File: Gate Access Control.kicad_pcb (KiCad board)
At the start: 2 copper layers, 85.1 x 38 mm, 20 parts, among them J1 Screw_Terminal_01x02, J2 RF Receiver 433MHz, J3 Conn_01x08, J4 IR_SENSORT, J5 Screw_Terminal_01x04, J6 Screw_Terminal_01x02, J7 Screw_Terminal_01x02, J8 Conn_01x06, U1 ATmega328-MM, Y1 Crystal

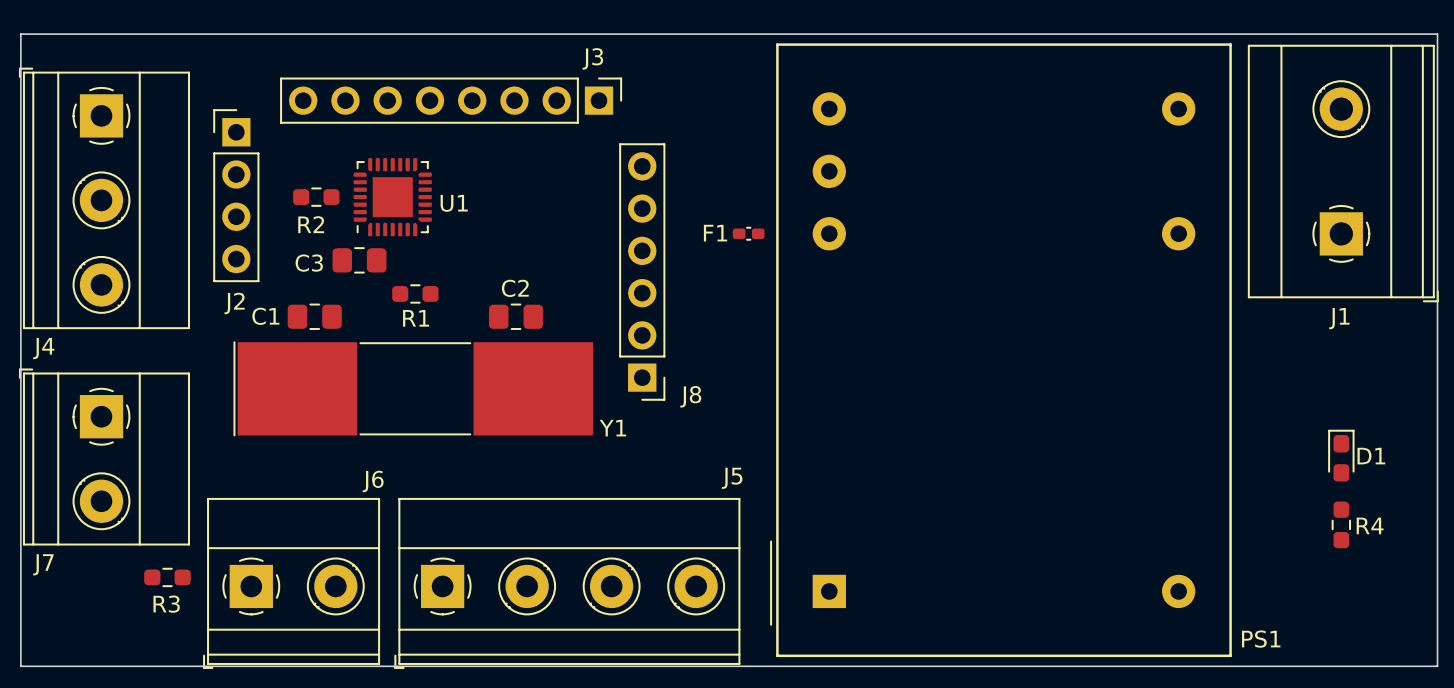
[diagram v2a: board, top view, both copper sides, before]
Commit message: Routed the Signal Traces
Design #1
Also changed on pre-defined size for Power to 0.25mm.
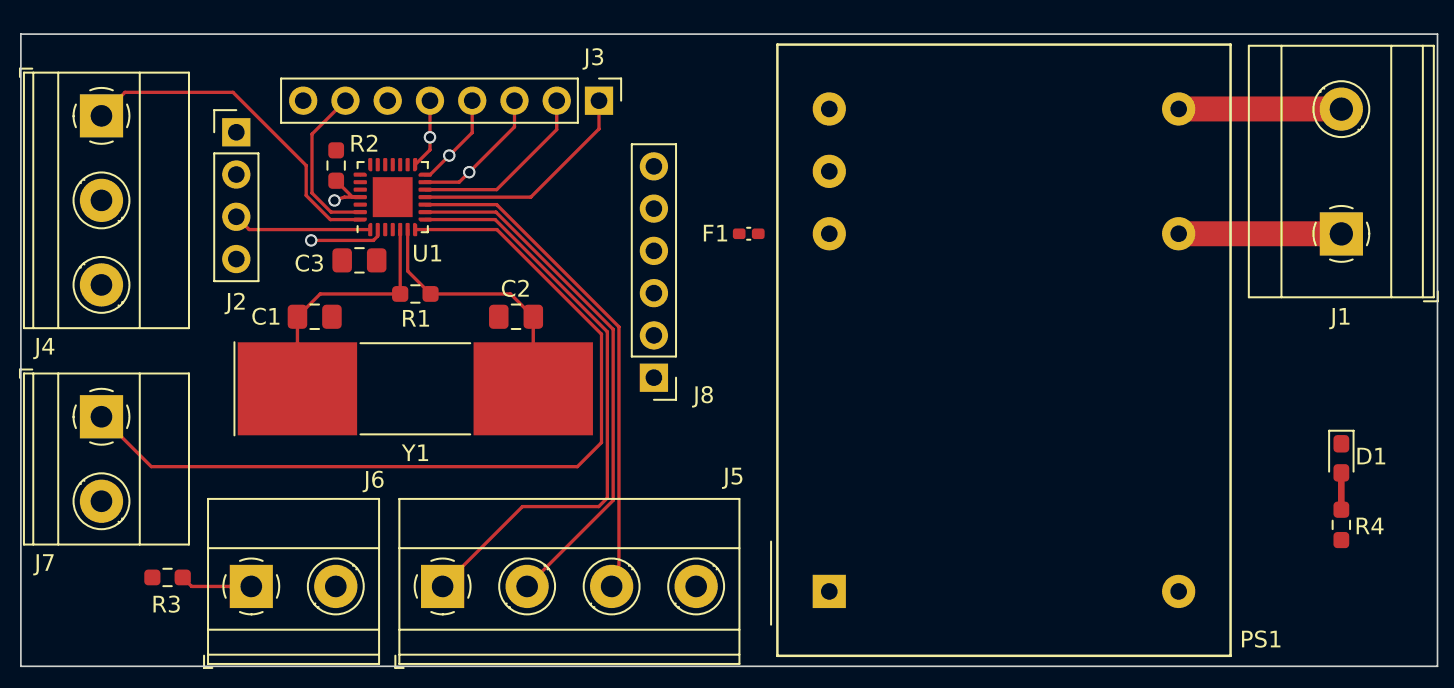
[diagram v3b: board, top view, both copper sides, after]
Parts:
- moved R2 2.24 mm to (71.5, 62.9), turned to 90 degrees
- moved J8 0.70 mm to (90.6, 75.7)
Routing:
- net /Flashing Lights: track 0.00 -> 52.2 mm
- net /Inverter PWM: track 0.00 -> 35.8 mm
- net /Enable: track 0.00 -> 31.8 mm
- net /DXN: track 0.00 -> 30.5 mm
- net /IR Sensor - DI: track 0.00 -> 20.4 mm
- net /XTAL2: track 0.00 -> 15.5 mm
- net /XTAL1: track 0.00 -> 14.9 mm
- net /RST: track 0.00 -> 13.8 mm
- net /SDA/SS: track 0.00 -> 11.1 mm
- net Net-(J1-Pin_1): track 0.00 -> 9.78 mm
- net Net-(J1-Pin_2): track 0.00 -> 9.78 mm
- net /IRQ: track 0.00 -> 9.76 mm
- net /Switch IN: track 0.00 -> 8.85 mm, vias 0 -> 1
- net /RF receiver - PWM: track 0.00 -> 8.37 mm
- net /MOSI: track 0.00 -> 8.33 mm, vias 0 -> 1
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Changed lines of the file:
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@@
   )
   (paper "A4")
+  (title_block
+    (title "George-PCB")
+  )
   (layers
     (0 "F.Cu" signal)
@@
   (net 31 "unconnected-(U1-PD0-Pad26)")
   (footprint "Connector_PinHeader_2.54mm:PinHeader_1x06_P2.54mm_Vertical" (layer "F.Cu")
-    (at 89.9 75.65 180)
+    (at 90.6 75.65 180)
     (descr "Through hole straight pin header, 1x06, 2.54mm pitch, single row")
     (tags "Through hole pin header THT 1x06 2.54mm single row")
@@
     (property "ki_keywords" "AVR 8bit Microcontroller MegaAVR")
     (attr smd)
-    (fp_text reference "U1" (at -0.4 3.7 180) (layer "F.SilkS")
+    (fp_text reference "U1" (at -3.4 2.1 180) (layer "F.SilkS")
         (effects (font (size 1 1) (thickness 0.15)))
     )
@@
     (property "ki_keywords" "quartz ceramic resonator oscillator")
     (attr smd)
-    (fp_text reference "Y1" (at 11.93875 2.4) (layer "F.SilkS")
+    (fp_text reference "Y1" (at 0.03875 3.88) (layer "F.SilkS")
         (effects (font (size 1 1) (thickness 0.15)))
     )
@@
   )
   (footprint "Resistor_SMD:R_0603_1608Metric_Pad0.98x0.95mm_HandSolder" (layer "F.Cu")
-    (at 70.31125 64.8 180)
+    (at 71.5 62.9 90)
     (descr "Resistor SMD 0603 (1608 Metric), square (rectangular) end terminal, IPC_7351 nominal with elongated pad for handsoldering. (Body size source: IPC-SM-782 page 72, https://www.pcb-3d.com/wordpress/wp-content/uploads/ipc-sm-782a_amendment_1_and_2.pdf), generated with kicad-footprint-generator")
     (tags "resistor handsolder")
@@
     (property "ki_keywords" "R res resistor")
     (attr smd)
-    (fp_text reference "R2" (at 0.31125 -1.7 180) (layer "F.SilkS")
-        (effects (font (size 1 1) (thickness 0.15)))
-    )
-    (fp_text value "1M" (at 0 1.43) (layer "F.Fab")
-        (effects (font (size 1 1) (thickness 0.15)))
-    )
-    (fp_text user "${REFERENCE}" (at 0 0) (layer "F.Fab")
+    (fp_text reference "R2" (at 1.3 1.7 180) (layer "F.SilkS")
+        (effects (font (size 1 1) (thickness 0.15)))
+    )
+    (fp_text value "1M" (at 0 1.43 90) (layer "F.Fab")
+        (effects (font (size 1 1) (thickness 0.15)))
+    )
+    (fp_text user "${REFERENCE}" (at 0 0 90) (layer "F.Fab")
         (effects (font (size 0.4 0.4) (thickness 0.06)))
     )
@@
     (fp_line (start 0.8 0.4125) (end -0.8 0.4125)
       (stroke (width 0.1) (type solid)) (layer "F.Fab"))
-    (pad "1" smd roundrect (at -0.9125 0 180) (size 0.975 0.95) (layers "F.Cu" "F.Paste" "F.Mask") (roundrect_rratio 0.25)
+    (pad "1" smd roundrect (at -0.9125 0 90) (size 0.975 0.95) (layers "F.Cu" "F.Paste" "F.Mask") (roundrect_rratio 0.25)
       (net 24 "/RESET") (pintype "passive"))
-    (pad "2" smd roundrect (at 0.9125 0 180) (size 0.975 0.95) (layers "F.Cu" "F.Paste" "F.Mask") (roundrect_rratio 0.25)
+    (pad "2" smd roundrect (at 0.9125 0 90) (size 0.975 0.95) (layers "F.Cu" "F.Paste" "F.Mask") (roundrect_rratio 0.25)
       (net 4 "+5V") (pintype "passive"))
     (model "${KICAD6_3DMODEL_DIR}/Resistor_SMD.3dshapes/R_0603_1608Metric.wrl"
@@
   (gr_rect (start 52.55 55) (end 137.7 93)
     (stroke (width 0.1) (type default)) (fill none) (layer "Edge.Cuts"))
+  (segment (start 69.17375 76.32) (end 69.17375 71.99) (width 0.2) (layer "F.Cu") (net 2))
+  (segment (start 70.54375 70.62) (end 75.35 70.62) (width 0.2) (layer "F.Cu") (net 2))
+  (segment (start 69.17375 71.99) (end 70.54375 70.62) (width 0.2) (layer "F.Cu") (net 2))
+  (segment (start 75.35 70.62) (end 75.35 66.75) (width 0.2) (layer "F.Cu") (net 2))
+  (segment (start 83.34875 76.32) (end 83.34875 71.9925) (width 0.2) (layer "F.Cu") (net 3))
+  (segment (start 77.175 70.62) (end 75.8 69.245) (width 0.2) (layer "F.Cu") (net 3))
+  (segment (start 75.8 69.245) (end 75.8 66.75) (width 0.2) (layer "F.Cu") (net 3))
+  (segment (start 81.98125 70.62) (end 83.35125 71.99) (width 0.2) (layer "F.Cu") (net 3))
+  (segment (start 83.34875 71.9925) (end 83.35125 71.99) (width 0.2) (layer "F.Cu") (net 3))
+  (segment (start 77.175 70.62) (end 81.98125 70.62) (width 0.2) (layer "F.Cu") (net 3))
+  (segment (start 131.92 81.375) (end 131.92 83.5875) (width 0.4) (layer "F.Cu") (net 5))
+  (segment (start 122.1425 67) (end 131.91 67) (width 1.5) (layer "F.Cu") (net 7))
+  (segment (start 131.91 67) (end 131.92 67.01) (width 1.5) (layer "F.Cu") (net 7))
+  (segment (start 122.1425 59.5) (end 131.91 59.5) (width 1.5) (layer "F.Cu") (net 8))
+  (segment (start 131.91 59.5) (end 131.92 59.51) (width 1.5) (layer "F.Cu") (net 8))
+  (segment (start 66.27 66.75) (end 73.55 66.75) (width 0.2) (layer "F.Cu") (net 10))
+  (segment (start 65.5 65.98) (end 66.27 66.75) (width 0.2) (layer "F.Cu") (net 10))
+  (segment (start 84.76 60.74) (end 81.15 64.35) (width 0.2) (layer "F.Cu") (net 11))
+  (segment (start 84.76 59) (end 84.76 60.74) (width 0.2) (layer "F.Cu") (net 11))
+  (segment (start 81.15 64.35) (end 76.85 64.35) (width 0.2) (layer "F.Cu") (net 11))
+  (segment (start 77.14 61.96) (end 76.25 62.85) (width 0.2) (layer "F.Cu") (net 12))
+  (segment (start 77.14 61.2) (end 77.14 61.96) (width 0.2) (layer "F.Cu") (net 12))
+  (segment (start 77.14 61.2) (end 77.14 59) (width 0.2) (layer "F.Cu") (net 12))
+  (via (at 77.14 61.2) (size 0.75) (drill 0.5) (layers "F.Cu" "B.Cu") (net 12))
+  (segment (start 78.9 63.9) (end 76.85 63.9) (width 0.2) (layer "F.Cu") (net 13))
+  (segment (start 79.5 63.3) (end 78.9 63.9) (width 0.2) (layer "F.Cu") (net 13))
+  (segment (start 82.22 60.58) (end 82.22 59) (width 0.2) (layer "F.Cu") (net 13))
+  (segment (start 79.5 63.3) (end 82.22 60.58) (width 0.2) (layer "F.Cu") (net 13))
+  (via (at 79.5 63.3) (size 0.75) (drill 0.5) (layers "F.Cu" "B.Cu") (net 13))
+  (segment (start 79.68 60.92) (end 79.68 59) (width 0.2) (layer "F.Cu") (net 14))
+  (segment (start 77.15 63.45) (end 76.85 63.45) (width 0.2) (layer "F.Cu") (net 14))
+  (segment (start 78.3 62.3) (end 79.68 60.92) (width 0.2) (layer "F.Cu") (net 14))
+  (segment (start 78.3 62.3) (end 77.15 63.45) (width 0.2) (layer "F.Cu") (net 14))
+  (via (at 78.3 62.3) (size 0.75) (drill 0.5) (layers "F.Cu" "B.Cu") (net 14))
+  (segment (start 72.95 65.7) (end 71.194974 65.7) (width 0.2) (layer "F.Cu") (net 15))
+  (segment (start 70.05 61.01) (end 72.06 59) (width 0.2) (layer "F.Cu") (net 15))
+  (segment (start 70.05 64.555026) (end 70.05 61.01) (width 0.2) (layer "F.Cu") (net 15))
+  (segment (start 71.194974 65.7) (end 70.05 64.555026) (width 0.2) (layer "F.Cu") (net 15))
+  (segment (start 76.85 64.8) (end 83.2 64.8) (width 0.2) (layer "F.Cu") (net 16))
+  (segment (start 87.3 60.7) (end 87.3 59) (width 0.2) (layer "F.Cu") (net 16))
+  (segment (start 83.2 64.8) (end 87.3 60.7) (width 0.2) (layer "F.Cu") (net 16))
+  (segment (start 71.15 66.15) (end 69.7 64.7) (width 0.2) (layer "F.Cu") (net 18))
+  (segment (start 58.81 58.5) (end 57.395 59.915) (width 0.2) (layer "F.Cu") (net 18))
+  (segment (start 69.7 64.7) (end 69.7 62.9) (width 0.2) (layer "F.Cu") (net 18))
+  (segment (start 69.7 62.9) (end 65.3 58.5) (width 0.2) (layer "F.Cu") (net 18))
+  (segment (start 65.3 58.5) (end 58.81 58.5) (width 0.2) (layer "F.Cu") (net 18))
+  (segment (start 72.95 66.15) (end 71.15 66.15) (width 0.2) (layer "F.Cu") (net 18))
+  (segment (start 88.15 72.744974) (end 88.15 83.03) (width 0.2) (layer "F.Cu") (net 19))
+  (segment (start 81.105026 65.7) (end 88.15 72.744974) (width 0.2) (layer "F.Cu") (net 19))
+  (segment (start 76.85 65.7) (end 81.105026 65.7) (width 0.2) (layer "F.Cu") (net 19))
+  (segment (start 88.15 83.03) (end 82.98 88.2) (width 0.2) (layer "F.Cu") (net 19))
+  (segment (start 82.7 83.4) (end 77.9 88.2) (width 0.2) (layer "F.Cu") (net 20))
+  (segment (start 87.8 82.885026) (end 87.285026 83.4) (width 0.2) (layer "F.Cu") (net 20))
+  (segment (start 81.060052 66.15) (end 87.8 72.889948) (width 0.2) (layer "F.Cu") (net 20))
+  (segment (start 87.285026 83.4) (end 82.7 83.4) (width 0.2) (layer "F.Cu") (net 20))
+  (segment (start 87.8 72.889948) (end 87.8 82.885026) (width 0.2) (layer "F.Cu") (net 20))
+  (segment (start 76.85 66.15) (end 81.060052 66.15) (width 0.2) (layer "F.Cu") (net 20))
+  (segment (start 81.15 65.25) (end 88.5 72.6) (width 0.2) (layer "F.Cu") (net 21))
+  (segment (start 88.5 87.76) (end 88.06 88.2) (width 0.2) (layer "F.Cu") (net 21))
+  (segment (start 88.5 72.6) (end 88.5 87.76) (width 0.2) (layer "F.Cu") (net 21))
+  (segment (start 76.85 65.25) (end 81.15 65.25) (width 0.2) (layer "F.Cu") (net 21))
+  (segment (start 73.741942 67.4) (end 70 67.4) (width 0.2) (layer "F.Cu") (net 22))
+  (segment (start 74 66.75) (end 74 67.141942) (width 0.2) (layer "F.Cu") (net 22))
+  (segment (start 74 67.141942) (end 73.741942 67.4) (width 0.2) (layer "F.Cu") (net 22))
+  (segment (start 62.2775 87.66) (end 62.8175 88.2) (width 0.2) (layer "F.Cu") (net 22))
+  (segment (start 62.8175 88.2) (end 66.4 88.2) (width 0.2) (layer "F.Cu") (net 22))
+  (via (at 70 67.4) (size 0.75) (drill 0.5) (layers "F.Cu" "B.Cu") (net 22))
+  (segment (start 87.45 79.55) (end 86 81) (width 0.2) (layer "F.Cu") (net 23))
+  (segment (start 76.25 66.75) (end 81.165078 66.75) (width 0.2) (layer "F.Cu") (net 23))
+  (segment (start 60.395 81) (end 57.395 78) (width 0.2) (layer "F.Cu") (net 23))
+  (segment (start 86 81) (end 60.395 81) (width 0.2) (layer "F.Cu") (net 23))
+  (segment (start 81.165078 66.75) (end 87.45 73.034922) (width 0.2) (layer "F.Cu") (net 23))
+  (segment (start 87.45 73.034922) (end 87.45 79.55) (width 0.2) (layer "F.Cu") (net 23))
+  (segment (start 72.4875 64.8) (end 71.5 63.8125) (width 0.2) (layer "F.Cu") (net 24))
+  (segment (start 72.95 64.8) (end 72 64.8) (width 0.2) (layer "F.Cu") (net 24))
+  (segment (start 71.4 65) (end 71.6 65.2) (width 0.2) (layer "F.Cu") (net 24))
+  (segment (start 72 64.8) (end 71.4 65) (width 0.2) (layer "F.Cu") (net 24))
+  (segment (start 72.95 64.8) (end 72.4875 64.8) (width 0.2) (layer "F.Cu") (net 24))
+  (via (at 71.4 65) (size 0.75) (drill 0.5) (layers "F.Cu" "B.Cu") (net 24))
 )

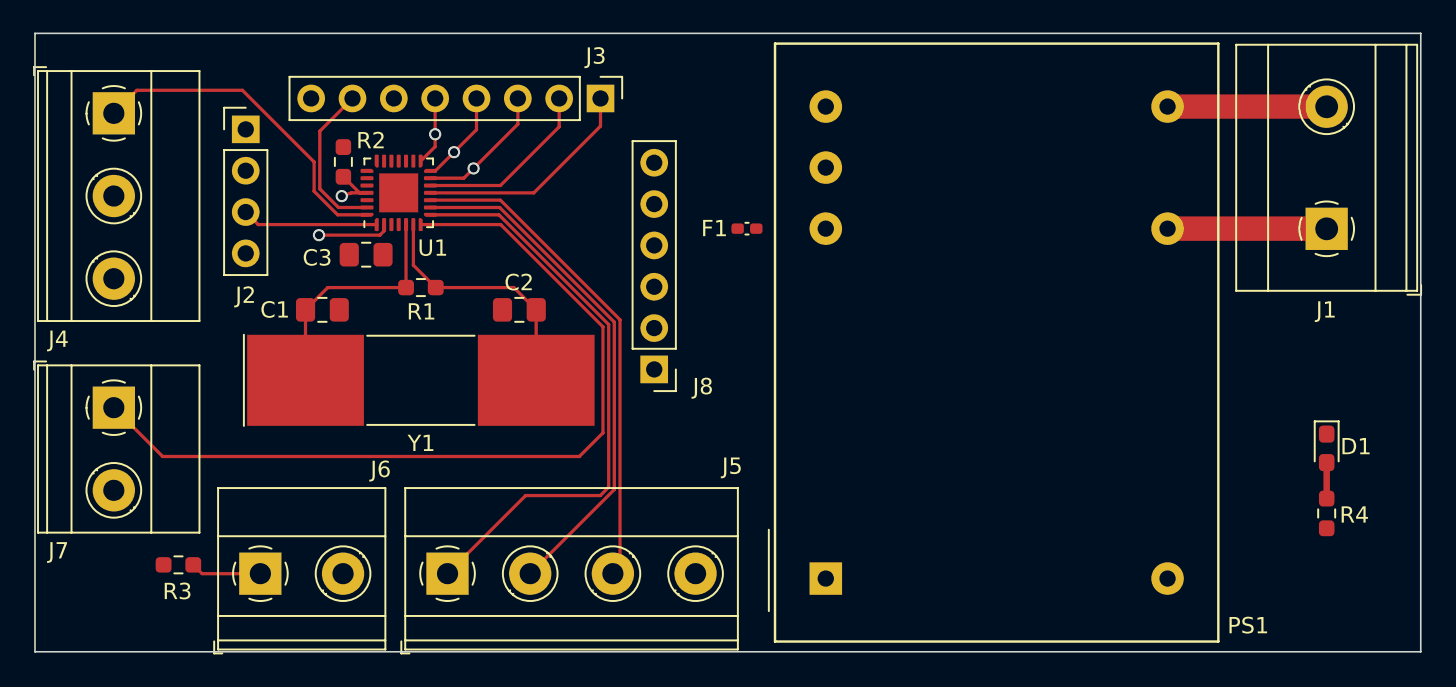
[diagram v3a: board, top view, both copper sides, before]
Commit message: Routed All Traces
Design #1
Added Ground Plane.
Also changed on pre-defined size for power to 0.25mm (not done in previous commit).
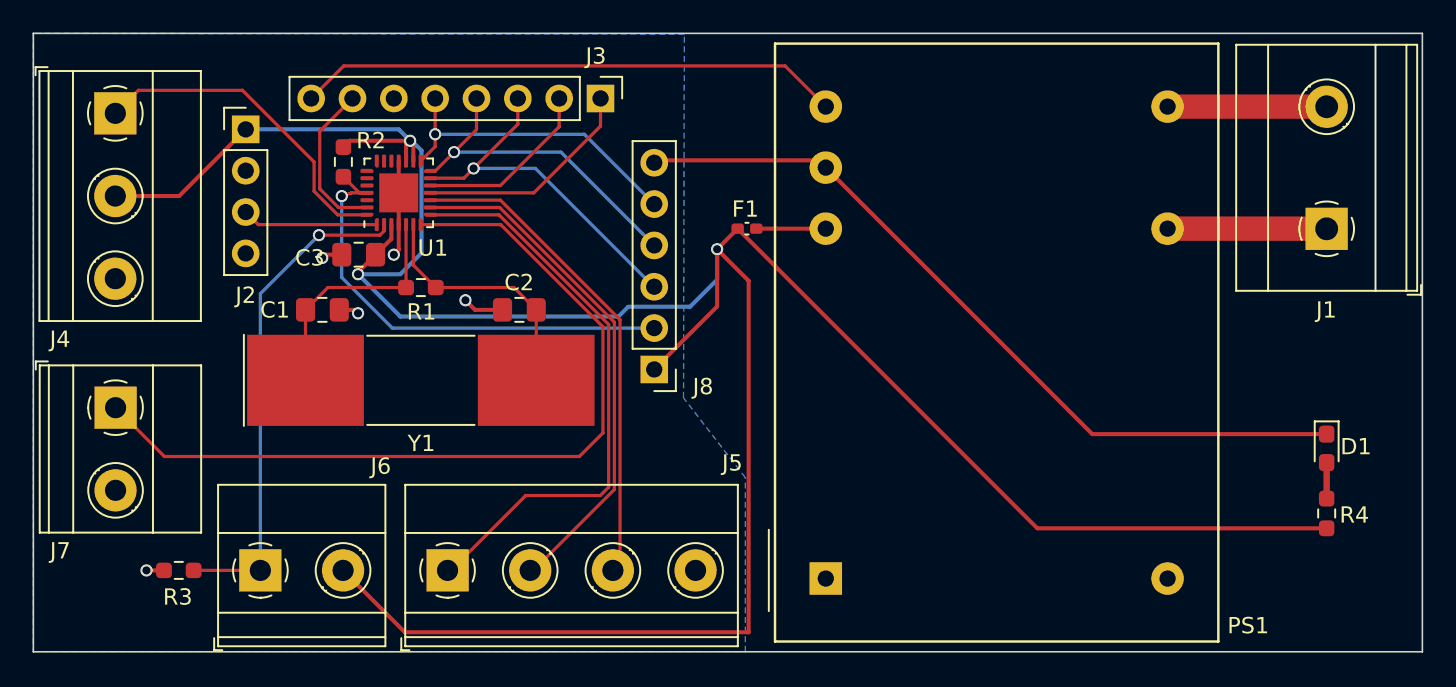
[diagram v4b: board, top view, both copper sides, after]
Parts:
- moved C3 0.46 mm to (72.4, 68.6)
- moved R3 0.34 mm to (61.4, 88.0)
- moved J5 0.20 mm to (77.9, 88.0)
- moved J6 0.20 mm to (66.4, 88.0)
- moved J7 0.10 mm to (57.5, 78.0)
- moved J4 0.09 mm to (57.5, 59.9)
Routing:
- net +5V: track 0.00 -> 174.0 mm, vias 0 -> 3
- net GND: track 0.00 -> 60.3 mm, vias 0 -> 5
- net +3.3V: track 0.00 -> 33.5 mm
- net /RESET: track 3.72 -> 28.9 mm
- net /Switch IN: track 8.85 -> 30.7 mm
- net /SCK: track 4.22 -> 19.5 mm
- net /MISO: track 5.80 -> 20.5 mm
- net /MOSI: track 8.33 -> 22.4 mm
- net Net-(PS1-Vout1): track 0.00 -> 4.27 mm
- added copper zone on B.Cu, net GND
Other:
- board size 85.1 x 38 mm -> 85.4 x 38 mm
